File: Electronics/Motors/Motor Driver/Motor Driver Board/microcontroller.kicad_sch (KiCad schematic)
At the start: 61 parts, among them IC1 STM32H723ZGT6, IC2 TJA1057GT/3, IC3 ESDA6V1W5, IC4 ESDA6V1W5, J1 TYPE-C-31-M-12, J2 Screw_Terminal_01x02, J3 TC2030, SW1 SW_DIP_x02, U1 LSM6DS3, X1 25MHz_Clock, X2 32.768kHz_Clock

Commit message: PCB Schematic progress
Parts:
- removed IC3, IC4: ESDA6V1W5, SOT65P210X110-5N, symbol ESDA6V1W5:ESDA6V1W5
- removed J1: TYPE-C-31-M-12, MSL Footprints:HRO_TYPE-C-31-M-12, symbol TYPE-C-31-M-12:TYPE-C-31-M-12
- removed J3: TC2030, Connector:Tag-Connect_TC2030-IDC-FP_2x03_P1.27mm_Vertical, symbol Connector:Conn_ARM_SWD_TagConnect_TC2030
- added FB1: 120R@100MHz, Resistor_SMD:R_0402_1005Metric, symbol Device:FerriteBead_Small
- added J12: TC2030, Connector:Tag-Connect_TC2030-IDC-FP_2x03_P1.27mm_Vertical, symbol Connector:Conn_ARM_SWD_TagConnect_TC2030
- added J3: TYPE-C-31-M-12, MSL Footprints:HRO_TYPE-C-31-M-12, symbol TYPE-C-31-M-12:TYPE-C-31-M-12
- added U5, U6: USBLC6-4SC6-ES, Package_TO_SOT_SMD:SOT-23-6, symbol MSL_Symbols:USBLC6-4SC6-ES
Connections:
- net +3V3: now also FB1.2, J12.1 (VCC), U5.5 (VBUS); no longer C30.1, C31.1, IC1.33 (VDDA)
- net CC1: now also J3.A5 (CC1), U6.1 (IO1)
- net CC2: now also J3.B5 (CC2), U6.3 (IO2)
- net GND: now also J12.5 (GND), J3.A1_B12 (GND), J3.B1_A12 (GND), U5.2 (GND), U6.2 (GND)
- net NRST: now also J12.3 (~{RESET}), U5.6 (IO4)
- net SWCLK: now also J12.4 (SWCLK), U5.4 (IO3)
- net SWDIO: now also J12.2 (SWDIO), U5.3 (IO2)
- net SWO: now also J12.6 (SWO), U5.1 (IO1)
- net USB_DN: now also J3.A7 (DN1), J3.B7 (DN2), U6.6 (IO4)
- net USB_DP: now also J3.A6 (DP1), J3.B6 (DP2), U6.4 (IO3)
- net VBUS: now also J3.A4_B9 (VBUS), J3.B4_A9 (VBUS), U6.5 (VBUS)
- new net: C30.1, C31.1, FB1.1, IC1.33 (VDDA)
- new net: J3.S1 (SHIELD), J3.S2 (SHIELD), J3.S3 (SHIELD), J3.S4 (SHIELD)
- no-connect marks 14 -> 13

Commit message: PCB Schematics finished
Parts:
- renumbered C1 to C301, C2 to C302, C28 to C306, C29 to C307, C32 to C308, C30 to C309, C33 to C310, C31 to C311, C34 to C312, C35 to C313, C36 to C314, C37 to C315, C38 to C316, C39 to C317, C40 to C318, C41 to C319, C42 to C320, C27 to C321, C43 to C322, C44 to C323, C45 to C324, C26 to C325, C12 to C326, C13 to C327, D5 to D301, D6 to D302, D7 to D303, IC2 to IC301, IC1 to IC302, J12 to J301, J2 to J302, J3 to J303, S3 to S301, S2 to S302, S1 to S303, SW1 to SW301, U5 to U301, U1 to U302, U6 to U303, X1 to X301, X2 to X302
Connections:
- net CAN_RX: now also IC302.114 (PD0)
- net CAN_TX: now also IC302.115 (PD1)

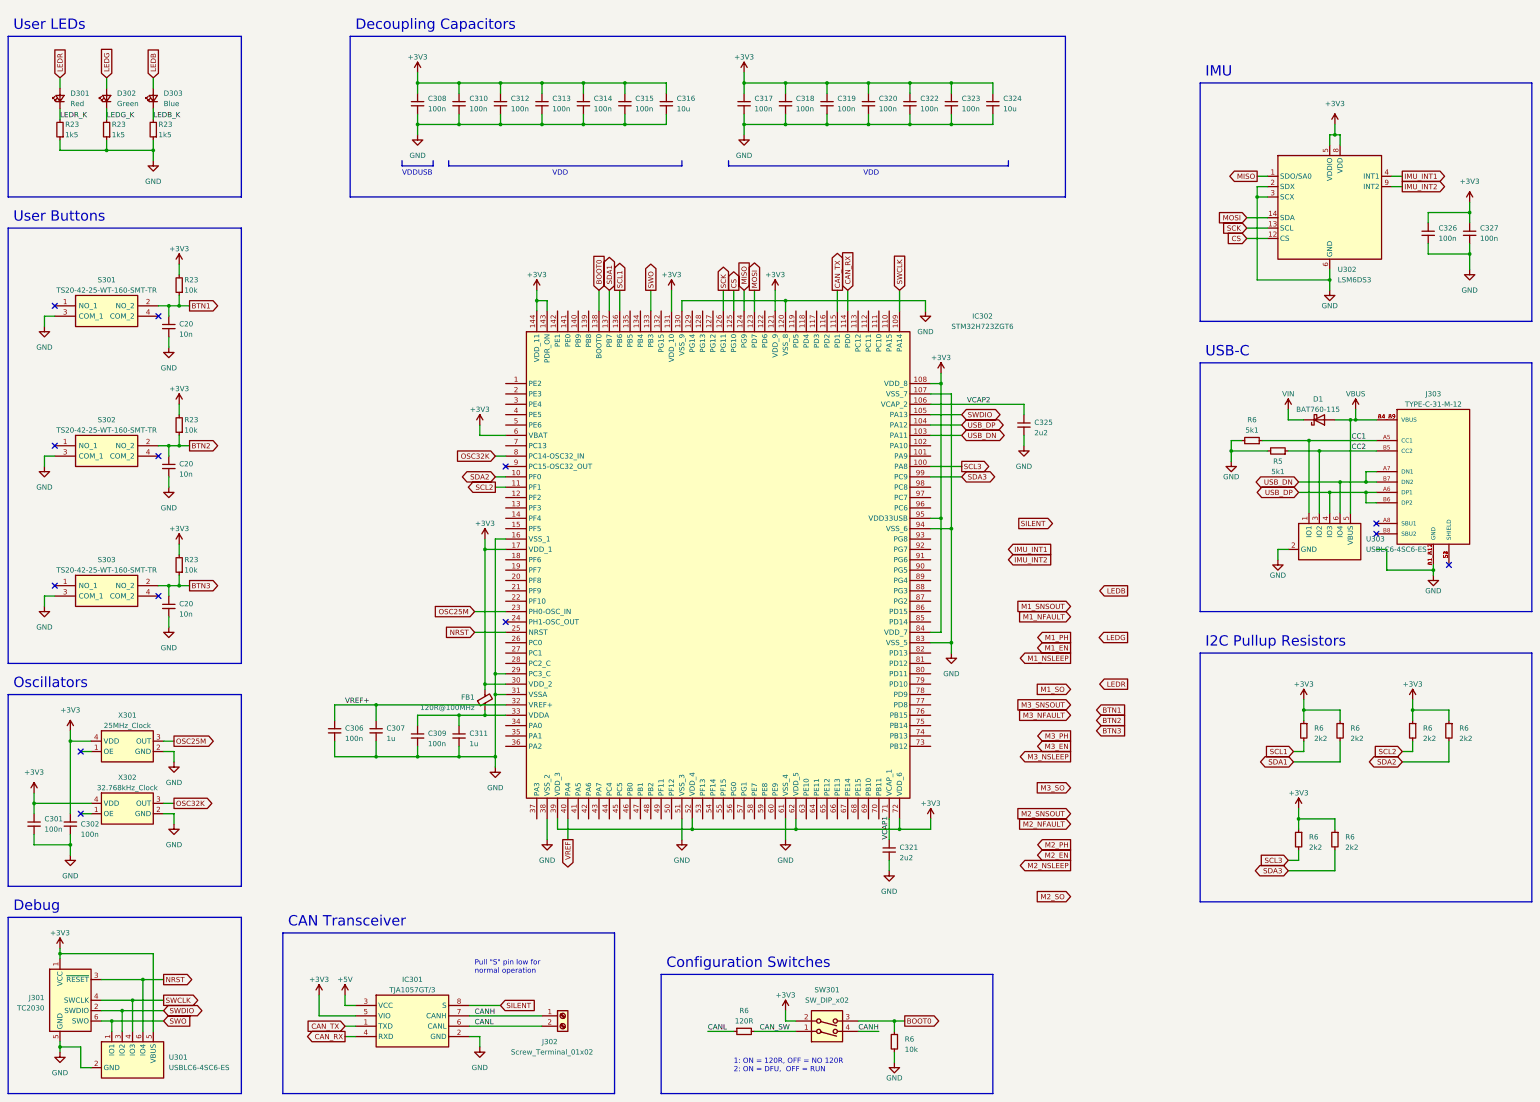
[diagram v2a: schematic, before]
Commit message: Schematic updates
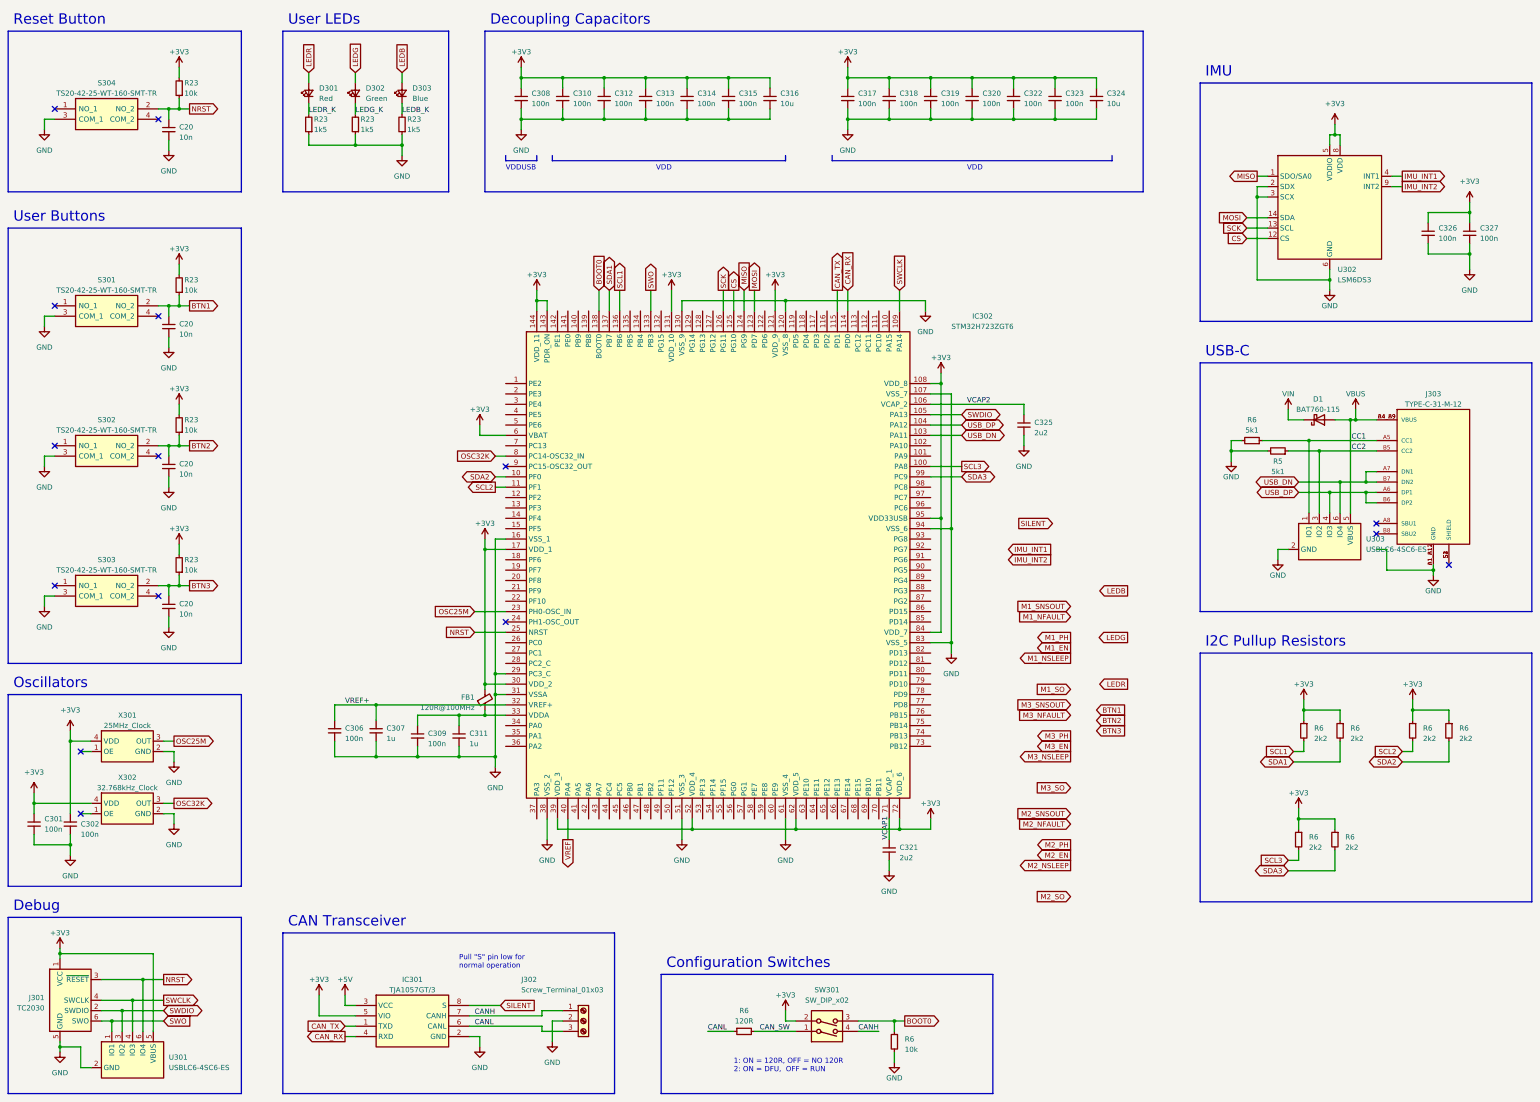
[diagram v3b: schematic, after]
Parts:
- removed J302: Screw_Terminal_01x02, TerminalBlock:TerminalBlock_bornier-2_P5.08mm, symbol Connector:Screw_Terminal_01x02
- added C20: 10n, Capacitor_SMD:C_0402_1005Metric, symbol Device:C_Small
- added J302: Screw_Terminal_01x03, TerminalBlock:TerminalBlock_bornier-3_P5.08mm, symbol Connector:Screw_Terminal_01x03
- added R23: 10k, Resistor_SMD:R_0402_1005Metric, symbol Device:R_Small
- added S304: TS20-42-25-WT-160-SMT-TR, MSL Footprints:TS204225WT160SMTTRMSL, symbol TS20-42-25-WT-160-SMT-TR-MSL:TS20-42-25-WT-160-SMT-TR
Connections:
- net +3V3: now also R23.2
- net CANH: now also J302.1 (Pin_1)
- net CANL: now also J302.3 (Pin_3)
- net GND: now also C20.2, J302.2 (Pin_2), S304.3 (COM_1)
- net NRST: now also C20.1, R23.1, S304.2 (NO_2)
- no-connect marks 13 -> 15
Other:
- note added: "Reset Button"
- moved on the sheet: C308, C310, C312, C313, C314, C315, C316, C317, C318, C319, C320, C322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

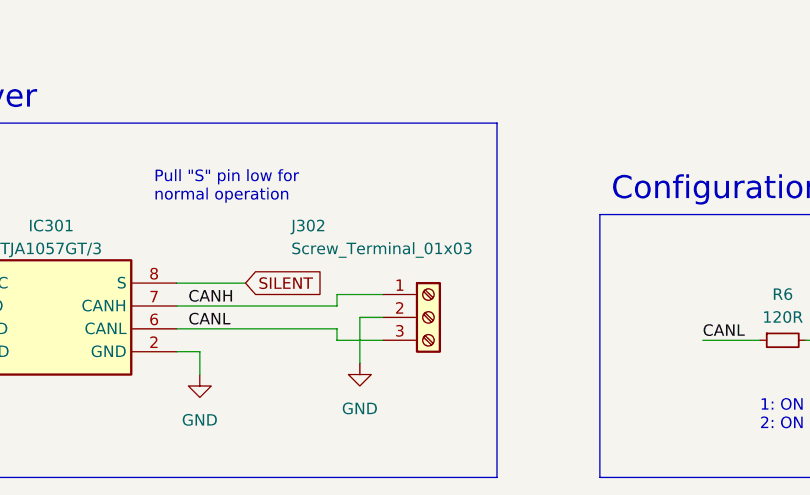
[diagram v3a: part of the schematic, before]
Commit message: PCB layout progress, spice simulations for power board
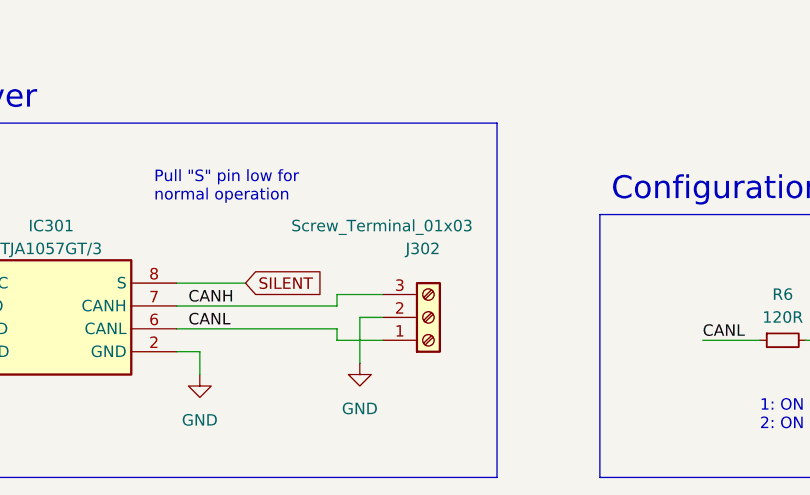
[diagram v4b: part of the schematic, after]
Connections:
- net CANH: now also J302.3 (Pin_3); no longer J302.1 (Pin_1)
- net CANL: now also J302.1 (Pin_1); no longer J302.3 (Pin_3)
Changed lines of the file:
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@@
     )
   )
+  (symbol (lib_id "Connector:Screw_Terminal_01x03") (at 160.02 261.62 0) (mirror x) (unit 1)
+    (in_bom yes) (on_board yes) (dnp no)
+    (property "Reference" "J302" (at 157.48 254 0)
+      (effects (font (size 1.27 1.27)) (justify left))
+    )
+    (property "Value" "Screw_Terminal_01x03" (at 144.78 251.46 0)
+      (effects (font (size 1.27 1.27)) (justify left))
+    )
+    (property "Footprint" "TerminalBlock:TerminalBlock_bornier-3_P5.08mm" (at 160.02 261.62 0)
+      (effects (font (size 1.27 1.27)) hide)
+    )
+    (property "Datasheet" "~" (at 160.02 261.62 0)
+      (effects (font (size 1.27 1.27)) hide)
+    )
+    (pin "1")
+    (pin "2")
+    (pin "3")
+    (instances
+      (project "Motor Driver Board"
+        (path "/5318664d-e328-4e84-a383-7318275dc447/86a04d6c-5487-4291-b767-6da69e96f7da"
+          (reference "J302") (unit 1)
+        )
+      )
+      (project "Power Board"
+        (path "/d8843e0a-fd8a-4193-ba57-f0164156e030/fab43204-4de8-48e9-a4c9-80bcd4a9c27a"
+          (reference "J303") (unit 1)
+        )
+      )
+    )
+  )
   (symbol (lib_id "power:+3V3") (at 95.25 255.27 0) (unit 1)
     (in_bom yes) (on_board yes) (dnp no) (fields_autoplaced)
@@
         )
       )
-    )
-  )
-  (symbol (lib_id "Connector:Screw_Terminal_01x03") (at 160.02 261.62 0) (unit 1)
-    (in_bom yes) (on_board yes) (dnp no)
-    (property "Reference" "J302" (at 144.78 251.46 0)
-      (effects (font (size 1.27 1.27)) (justify left))
-    )
-    (property "Value" "Screw_Terminal_01x03" (at 144.78 254 0)
-      (effects (font (size 1.27 1.27)) (justify left))
-    )
-    (property "Footprint" "TerminalBlock:TerminalBlock_bornier-3_P5.08mm" (at 160.02 261.62 0)
-      (effects (font (size 1.27 1.27)) hide)
-    )
-    (property "Datasheet" "~" (at 160.02 261.62 0)
-      (effects (font (size 1.27 1.27)) hide)
-    )
-    (pin "1")
-    (pin "2")
-    (pin "3")
-    (instances
-      (project "Motor Driver Board"
-        (path "/5318664d-e328-4e84-a383-7318275dc447/86a04d6c-5487-4291-b767-6da69e96f7da"
-          (reference "J302") (unit 1)
-        )
-      )
-      (project "Power Board"
-        (path "/d8843e0a-fd8a-4193-ba57-f0164156e030/fab43204-4de8-48e9-a4c9-80bcd4a9c27a"
-          (reference "J303") (unit 1)
-        )
-      )

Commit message: Finished power board layout
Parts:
- U301: now not fitted; now left out of the parts list
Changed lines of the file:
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@@
   )
   (symbol (lib_id "MSL_Symbols:USBLC6-4SC6-ES") (at 49.53 271.78 0) (unit 1)
-    (in_bom yes) (on_board yes) (dnp no) (fields_autoplaced)
+    (in_bom no) (on_board no) (dnp yes) (fields_autoplaced)
     (property "Reference" "U301" (at 58.42 270.51 0)
       (effects (font (size 1.27 1.27)) (justify left))
